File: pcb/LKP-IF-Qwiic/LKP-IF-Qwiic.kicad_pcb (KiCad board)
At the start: 2 copper layers, 41 x 36 mm, 8 parts, among them J1 JST SH, J2 JST SH, J3 LKP SWD .1" Extra Long, J4 LKP I/O .1" Extra Long, U1 TCA9406DCTR

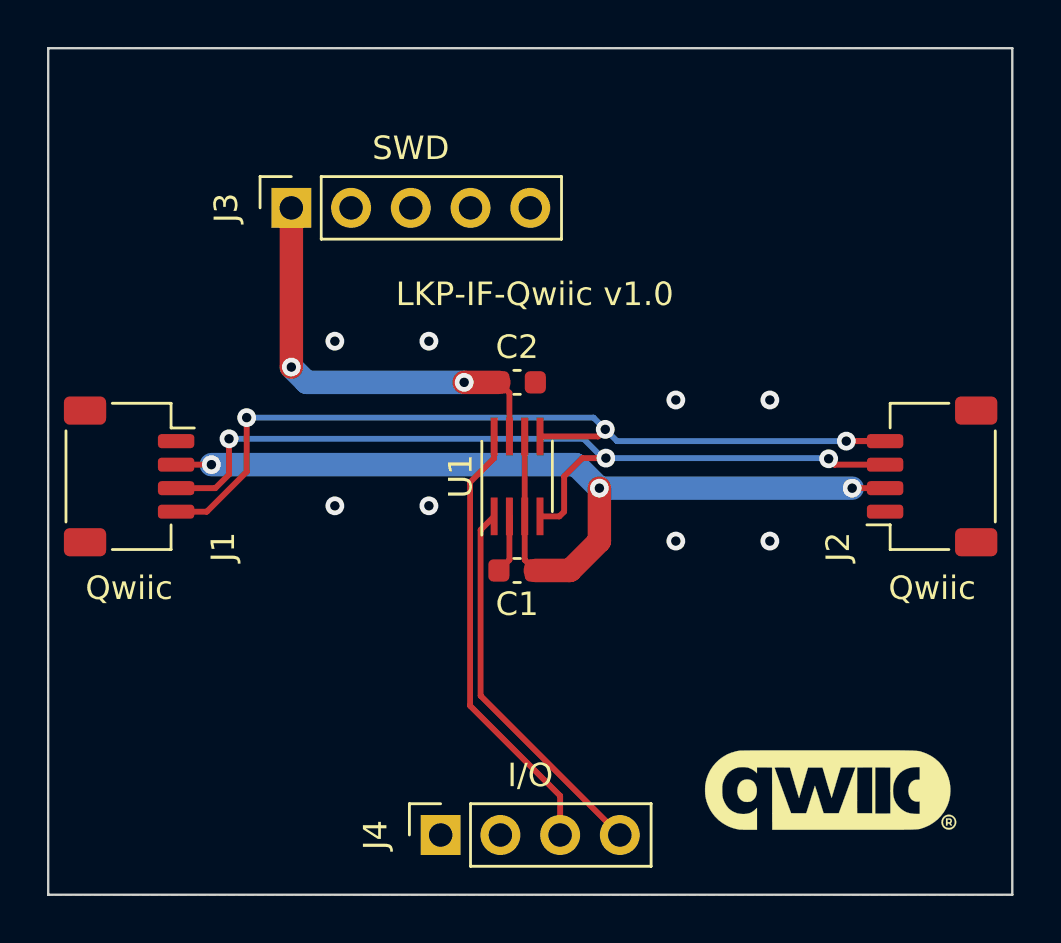
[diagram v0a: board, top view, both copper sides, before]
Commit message: LKP-IF-Qwiic: Add reverse voltage protection.
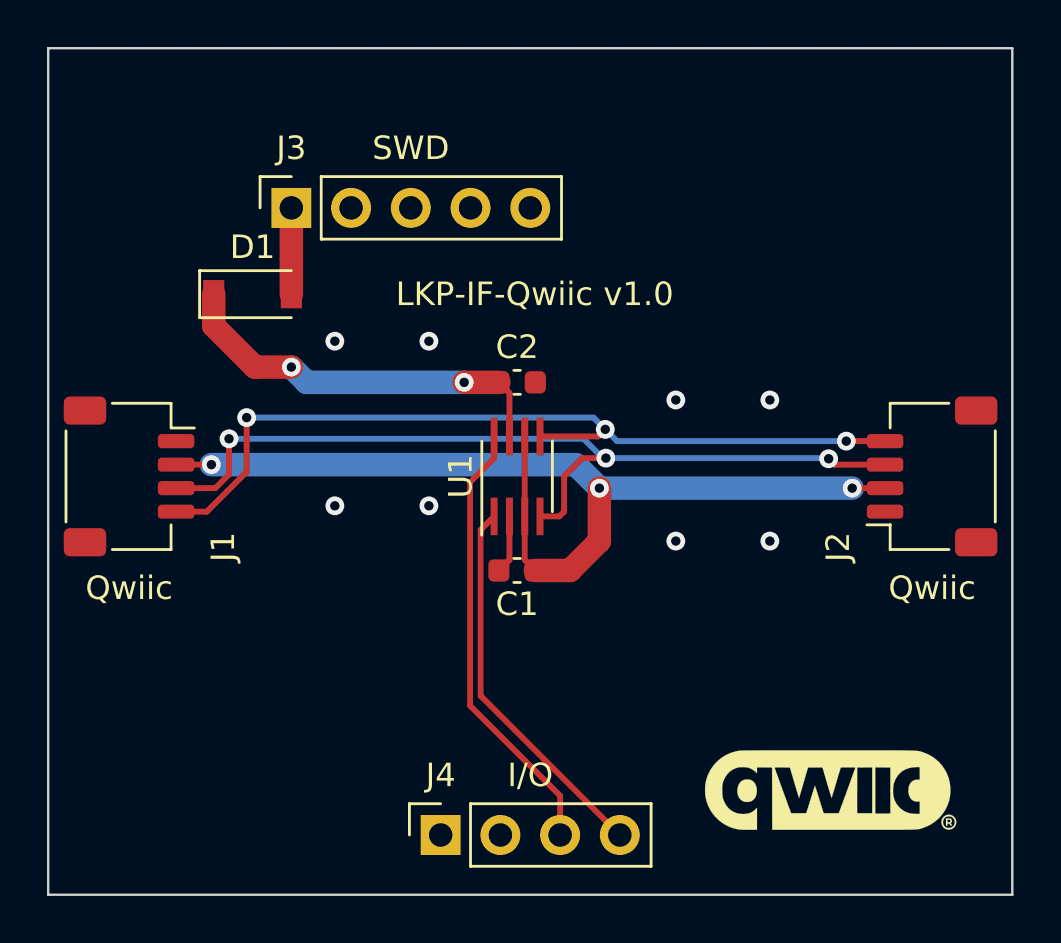
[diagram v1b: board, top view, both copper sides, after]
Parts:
- added D1: MBR0520L, Diode_SMD:D_SOD-123, F.Cu at (138.7, 90.5)
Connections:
- J3 pad 1: +5V -> Net-(D1-Pad2)
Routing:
- net Net-(D1-Pad2): track 0.00 -> 3.67 mm
- net +5V: track 18.4 -> 17.0 mm
